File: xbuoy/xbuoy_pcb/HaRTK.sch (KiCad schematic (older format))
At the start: 19 parts, among them J1 PWM0, J2 PWM1, J3 PWM2, J4 PWM3, J5 Gen, J6 BINR, P1 Telem RF, P2 GPS RF, P5 Bat holder, U1 RaspberryPi, U2 TLV70233_SOT23-5, U3 RFM22B, U4 NV08C-CSM

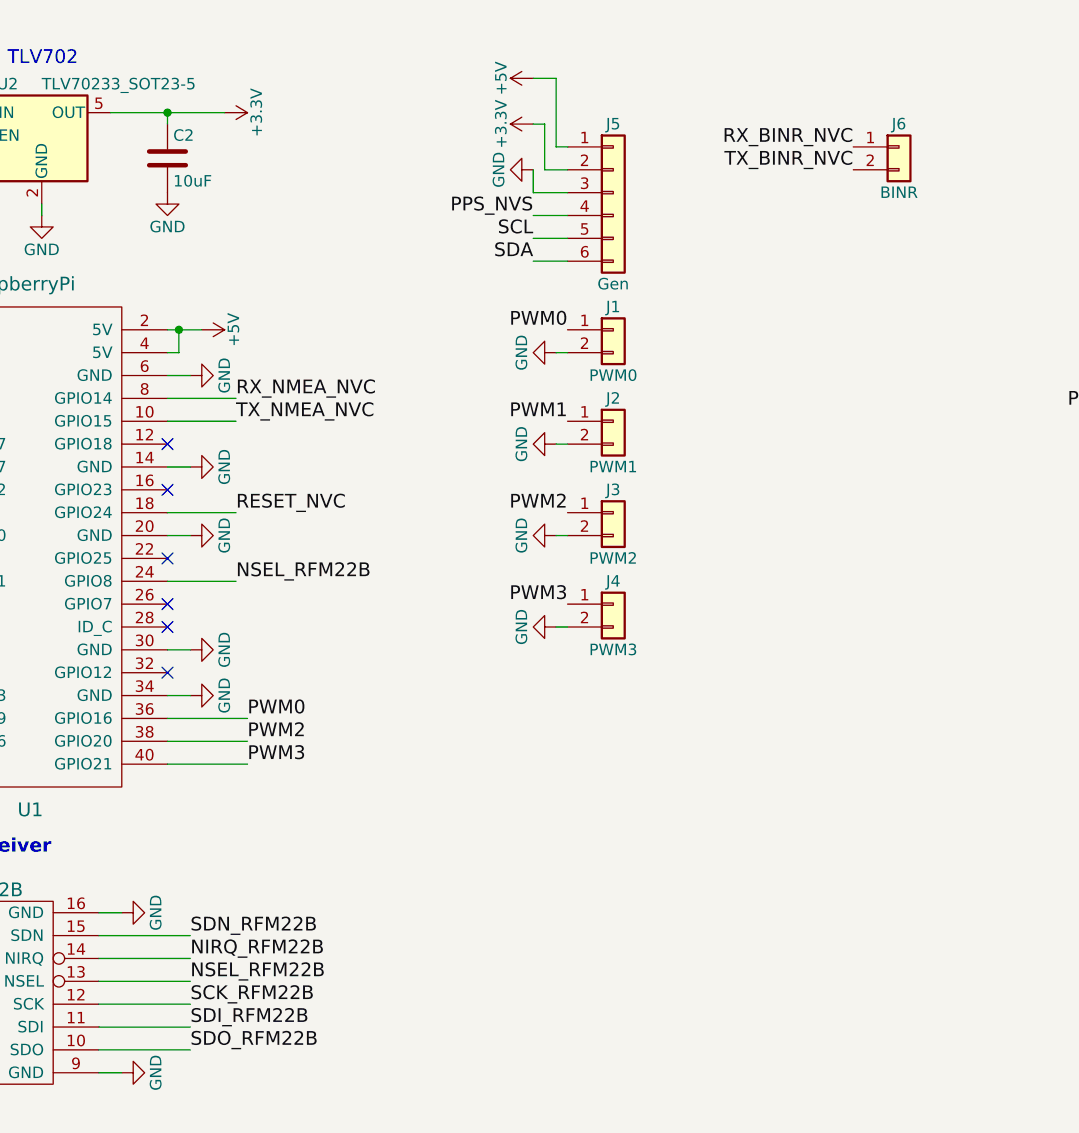
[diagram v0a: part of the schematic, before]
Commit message: Changed reset pin
Signed-off-by: hardiepienaar <hardiepienaar@gmail.com>
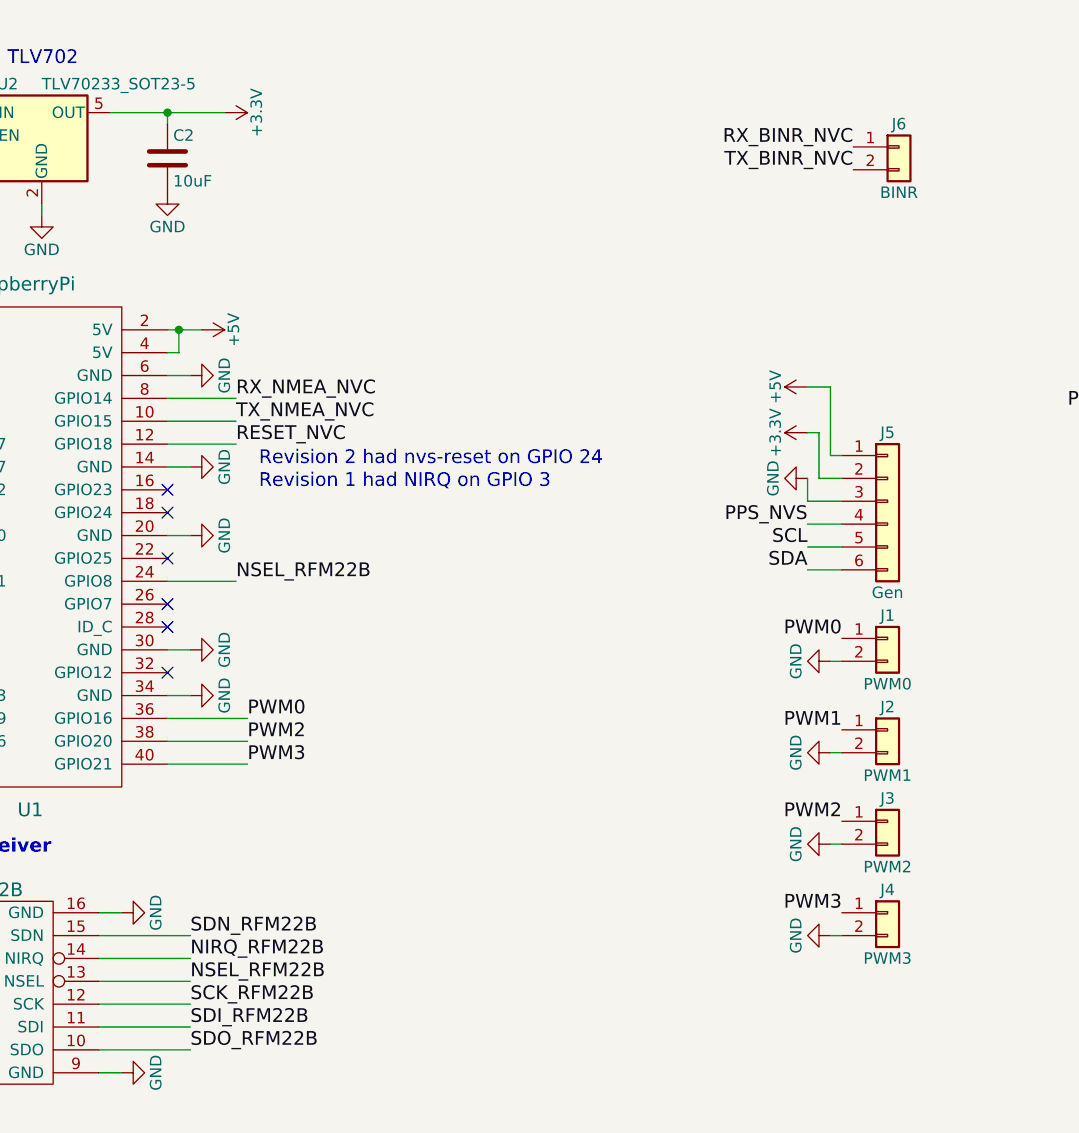
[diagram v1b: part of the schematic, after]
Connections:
- net RESET_NVC: now also U1.12 (GPIO18); no longer U1.18 (GPIO24)
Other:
- note added: "Revision 1 had NIRQ on GPIO 3\n"
- note added: "Revision 2 had nvs-reset on GPIO 24\n"
- moved on the sheet: J1, J2, J3, J4, J5
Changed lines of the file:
@@
 Text Notes 9600 2100 0    60   ~ 0
 Reset needs to be pulsed\nlonger than 1ms and will \nstay in reset 140ms after \nthe signal.
-Text Label 3050 2600 0    60   ~ 0
+Text Label 3050 2300 0    60   ~ 0
 RESET_NVC
 Text Label 7050 2150 2    60   ~ 0
 PPS_NVS
-Text Label 4350 1300 2    60   ~ 0
+Text Label 5550 2650 2    60   ~ 0
 PPS_NVS
 Text Notes 9800 4150 0    60   ~ 12
@@
 L GND #PWR040
 U 1 1 56FF0ED5
-P 4350 1100
-F 0 "#PWR040" H 4350 850 50  0001 C CNN
-F 1 "GND" H 4350 950 50  0000 C CNN
-F 2 "" H 4350 1100 50  0000 C CNN
-F 3 "" H 4350 1100 50  0000 C CNN
-	1    4350 1100
+P 5550 2450
+F 0 "#PWR040" H 5550 2200 50  0001 C CNN
+F 1 "GND" H 5550 2300 50  0000 C CNN
+F 2 "" H 5550 2450 50  0000 C CNN
+F 3 "" H 5550 2450 50  0000 C CNN
+	1    5550 2450
 	0    1    1    0
 $EndComp
 Wire Wire Line
-	4500 1500 4350 1500
+	5700 2850 5550 2850
 Wire Wire Line
-	4500 1400 4350 1400
+	5700 2750 5550 2750
 Text Notes 7650 2700 0    60   ~ 0
 Default: \nGPIO3: 0\nGPIO4: 0\nGPIO5: 0
@@
 Wire Wire Line
 	1550 2000 1250 2000
-Text Label 4350 1500 2    60   ~ 0
+Text Label 5550 2850 2    60   ~ 0
 SDA
-Text Label 4350 1400 2    60   ~ 0
+Text Label 5550 2750 2    60   ~ 0
 SCL
 $Comp
 L +3.3V #PWR041
 U 1 1 56FFC1C4
-P 4350 900
-F 0 "#PWR041" H 4350 750 50  0001 C CNN
-F 1 "+3.3V" H 4350 1040 50  0000 C CNN
-F 2 "" H 4350 900 50  0000 C CNN
-F 3 "" H 4350 900 50  0000 C CNN
-	1    4350 900
+P 5550 2250
+F 0 "#PWR041" H 5550 2100 50  0001 C CNN
+F 1 "+3.3V" H 5550 2390 50  0000 C CNN
+F 2 "" H 5550 2250 50  0000 C CNN
+F 3 "" H 5550 2250 50  0000 C CNN
+	1    5550 2250
 	0    -1   1    0
 $EndComp
 Wire Wire Line
-	4350 1300 4500 1300
+	5550 2650 5700 2650
 Wire Wire Line
-	4350 1200 4500 1200
+	5550 2550 5700 2550
 Wire Wire Line
-	4350 1200 4350 1100
+	5550 2550 5550 2450
 Text Notes 7400 6950 0    157  ~ 0
 Raspberry Pi Zero XBuoy Hat
@@
 L Conn_01x02 J1
 U 1 1 59D1039F
-P 4700 1800
-F 0 "J1" H 4700 1900 50  0000 C CNN
-F 1 "PWM0" H 4700 1600 50  0000 C CNN
-F 2 "Pin_Headers:Pin_Header_Straight_1x02_Pitch2.54mm" H 4700 1800 50  0001 C CNN
-F 3 "" H 4700 1800 50  0001 C CNN
-	1    4700 1800
+P 5900 3150
+F 0 "J1" H 5900 3250 50  0000 C CNN
+F 1 "PWM0" H 5900 2950 50  0000 C CNN
+F 2 "Pin_Headers:Pin_Header_Straight_1x02_Pitch2.54mm" H 5900 3150 50  0001 C CNN
+F 3 "" H 5900 3150 50  0001 C CNN
+	1    5900 3150
 	1    0    0    -1
 $EndComp
@@
 L Conn_01x02 J2
 U 1 1 59D104B6
-P 4700 2200
-F 0 "J2" H 4700 2300 50  0000 C CNN
-F 1 "PWM1" H 4700 2000 50  0000 C CNN
-F 2 "Pin_Headers:Pin_Header_Straight_1x02_Pitch2.54mm" H 4700 2200 50  0001 C CNN
-F 3 "" H 4700 2200 50  0001 C CNN
-	1    4700 2200
+P 5900 3550
+F 0 "J2" H 5900 3650 50  0000 C CNN
+F 1 "PWM1" H 5900 3350 50  0000 C CNN
+F 2 "Pin_Headers:Pin_Header_Straight_1x02_Pitch2.54mm" H 5900 3550 50  0001 C CNN
+F 3 "" H 5900 3550 50  0001 C CNN
+	1    5900 3550
 	1    0    0    -1
 $EndComp
@@
 L Conn_01x02 J3
 U 1 1 59D104F8
-P 4700 2600
-F 0 "J3" H 4700 2700 50  0000 C CNN
-F 1 "PWM2" H 4700 2400 50  0000 C CNN
-F 2 "Pin_Headers:Pin_Header_Straight_1x02_Pitch2.54mm" H 4700 2600 50  0001 C CNN
-F 3 "" H 4700 2600 50  0001 C CNN
-	1    4700 2600
+P 5900 3950
+F 0 "J3" H 5900 4050 50  0000 C CNN
+F 1 "PWM2" H 5900 3750 50  0000 C CNN
+F 2 "Pin_Headers:Pin_Header_Straight_1x02_Pitch2.54mm" H 5900 3950 50  0001 C CNN
+F 3 "" H 5900 3950 50  0001 C CNN
+	1    5900 3950
 	1    0    0    -1
 $EndComp
@@
 L Conn_01x02 J4
 U 1 1 59D1053B
-P 4700 3000
-F 0 "J4" H 4700 3100 50  0000 C CNN
-F 1 "PWM3" H 4700 2800 50  0000 C CNN
-F 2 "Pin_Headers:Pin_Header_Straight_1x02_Pitch2.54mm" H 4700 3000 50  0001 C CNN
-F 3 "" H 4700 3000 50  0001 C CNN
-	1    4700 3000
+P 5900 4350
+F 0 "J4" H 5900 4450 50  0000 C CNN
+F 1 "PWM3" H 5900 4150 50  0000 C CNN
+F 2 "Pin_Headers:Pin_Header_Straight_1x02_Pitch2.54mm" H 5900 4350 50  0001 C CNN
+F 3 "" H 5900 4350 50  0001 C CNN
+	1    5900 4350
 	1    0    0    -1
 $EndComp
@@
 L GND #PWR043
 U 1 1 59D107C7
-P 4450 3100
-F 0 "#PWR043" H 4450 2850 50  0001 C CNN
-F 1 "GND" H 4450 2950 50  0000 C CNN
-F 2 "" H 4450 3100 50  0000 C CNN
-F 3 "" H 4450 3100 50  0000 C CNN
-	1    4450 3100
+P 5650 4450
+F 0 "#PWR043" H 5650 4200 50  0001 C CNN
+F 1 "GND" H 5650 4300 50  0000 C CNN
+F 2 "" H 5650 4450 50  0000 C CNN
+F 3 "" H 5650 4450 50  0000 C CNN
+	1    5650 4450
 	0    1    1    0
 $EndComp
 Wire Wire Line
-	4450 3100 4500 3100
+	5650 4450 5700 4450
 $Comp
 L GND #PWR044
 U 1 1 59D10930
-P 4450 2700
-F 0 "#PWR044" H 4450 2450 50  0001 C CNN
-F 1 "GND" H 4450 2550 50  0000 C CNN
-F 2 "" H 4450 2700 50  0000 C CNN
-F 3 "" H 4450 2700 50  0000 C CNN
-	1    4450 2700
+P 5650 4050
+F 0 "#PWR044" H 5650 3800 50  0001 C CNN
+F 1 "GND" H 5650 3900 50  0000 C CNN
+F 2 "" H 5650 4050 50  0000 C CNN
+F 3 "" H 5650 4050 50  0000 C CNN
+	1    5650 4050
 	0    1    1    0
 $EndComp
 Wire Wire Line
-	4450 2700 4500 2700
+	5650 4050 5700 4050
 $Comp
 L GND #PWR045
 U 1 1 59D109EA
-P 4450 2300
-F 0 "#PWR045" H 4450 2050 50  0001 C CNN
-F 1 "GND" H 4450 2150 50  0000 C CNN
-F 2 "" H 4450 2300 50  0000 C CNN
-F 3 "" H 4450 2300 50  0000 C CNN
-	1    4450 2300
+P 5650 3650
+F 0 "#PWR045" H 5650 3400 50  0001 C CNN
+F 1 "GND" H 5650 3500 50  0000 C CNN
+F 2 "" H 5650 3650 50  0000 C CNN
+F 3 "" H 5650 3650 50  0000 C CNN
+	1    5650 3650
 	0    1    1    0
 $EndComp
 Wire Wire Line
-	4450 2300 4500 2300
+	5650 3650 5700 3650
 $Comp
 L GND #PWR046
 U 1 1 59D10AA5
-P 4450 1900
-F 0 "#PWR046" H 4450 1650 50  0001 C CNN
-F 1 "GND" H 4450 1750 50  0000 C CNN
-F 2 "" H 4450 1900 50  0000 C CNN
-F 3 "" H 4450 1900 50  0000 C CNN
-	1    4450 1900
+P 5650 3250
+F 0 "#PWR046" H 5650 3000 50  0001 C CNN
+F 1 "GND" H 5650 3100 50  0000 C CNN
+F 2 "" H 5650 3250 50  0000 C CNN
+F 3 "" H 5650 3250 50  0000 C CNN
+	1    5650 3250
 	0    1    1    0
 $EndComp
 Wire Wire Line
-	4450 1900 4500 1900
-Text Label 4500 1800 2    60   ~ 0
+	5650 3250 5700 3250
+Text Label 5700 3150 2    60   ~ 0
 PWM0
-Text Label 4500 2200 2    60   ~ 0
+Text Label 5700 3550 2    60   ~ 0
 PWM1
-Text Label 4500 2600 2    60   ~ 0
+Text Label 5700 3950 2    60   ~ 0
 PWM2
-Text Label 4500 3000 2    60   ~ 0
+Text Label 5700 4350 2    60   ~ 0
 PWM3
 Text Label 3100 3500 0    60   ~ 0
@@
 L +5V #PWR047
 U 1 1 59D15EC1
-P 4350 700
-F 0 "#PWR047" H 4350 550 50  0001 C CNN
-F 1 "+5V" H 4350 840 50  0000 C CNN
-F 2 "" H 4350 700 50  0000 C CNN
-F 3 "" H 4350 700 50  0000 C CNN
-	1    4350 700
+P 5550 2050
+F 0 "#PWR047" H 5550 1900 50  0001 C CNN
+F 1 "+5V" H 5550 2190 50  0000 C CNN
+F 2 "" H 5550 2050 50  0000 C CNN
+F 3 "" H 5550 2050 50  0000 C CNN
+	1    5550 2050
 	0    -1   -1   0
 $EndComp
 Wire Wire Line
-	4350 900  4400 900
+	5550 2250 5600 2250
 Wire Wire Line
-	4400 900  4400 1100
+	5600 2250 5600 2450
 Wire Wire Line
-	4400 1100 4500 1100
+	5600 2450 5700 2450
 Wire Wire Line
-	4350 700  4450 700
+	5550 2050 5650 2050
 Wire Wire Line
-	4450 700  4450 1000
+	5650 2050 5650 2350
 Wire Wire Line
-	4450 1000 4500 1000
+	5650 2350 5700 2350
 $Comp
 L Conn_01x06 J5
 U 1 1 59D15FF5
-P 4700 1200
-F 0 "J5" H 4700 1500 50  0000 C CNN
-F 1 "Gen" H 4700 800 50  0000 C CNN
-F 2 "Pin_Headers:Pin_Header_Straight_1x06_Pitch2.54mm" H 4700 1200 50  0001 C CNN
-F 3 "" H 4700 1200 50  0001 C CNN
-	1    4700 1200
+P 5900 2550
+F 0 "J5" H 5900 2850 50  0000 C CNN
+F 1 "Gen" H 5900 2150 50  0000 C CNN
+F 2 "Pin_Headers:Pin_Header_Straight_1x06_Pitch2.54mm" H 5900 2550 50  0001 C CNN
+F 3 "" H 5900 2550 50  0001 C CNN
+	1    5900 2550
 	1    0    0    -1
 $EndComp
@@
 	1    0    0    -1
 $EndComp
-Wire Wire Line
-	3050 2600 2750 2600
 $Comp
 L GND #PWR048
@@
 NoConn ~ 1550 2400
 NoConn ~ 1550 2500
-NoConn ~ 2750 2300
 NoConn ~ 2750 2500
 NoConn ~ 2750 2800
@@
 NoConn ~ 9000 2650
 NoConn ~ 1550 1800
+Wire Wire Line
+	2750 2300 3050 2300
+NoConn ~ 2750 2600
+Text Notes 3150 2400 0    60   ~ 0
+Revision 2 had nvs-reset on GPIO 24\n
+Text Notes 3150 2500 0    60   ~ 0
+Revision 1 had NIRQ on GPIO 3\n
 $EndSCHEMATC
